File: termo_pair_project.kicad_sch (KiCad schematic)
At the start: 25 parts, among them P1 503, P2 503, U2 NE5532

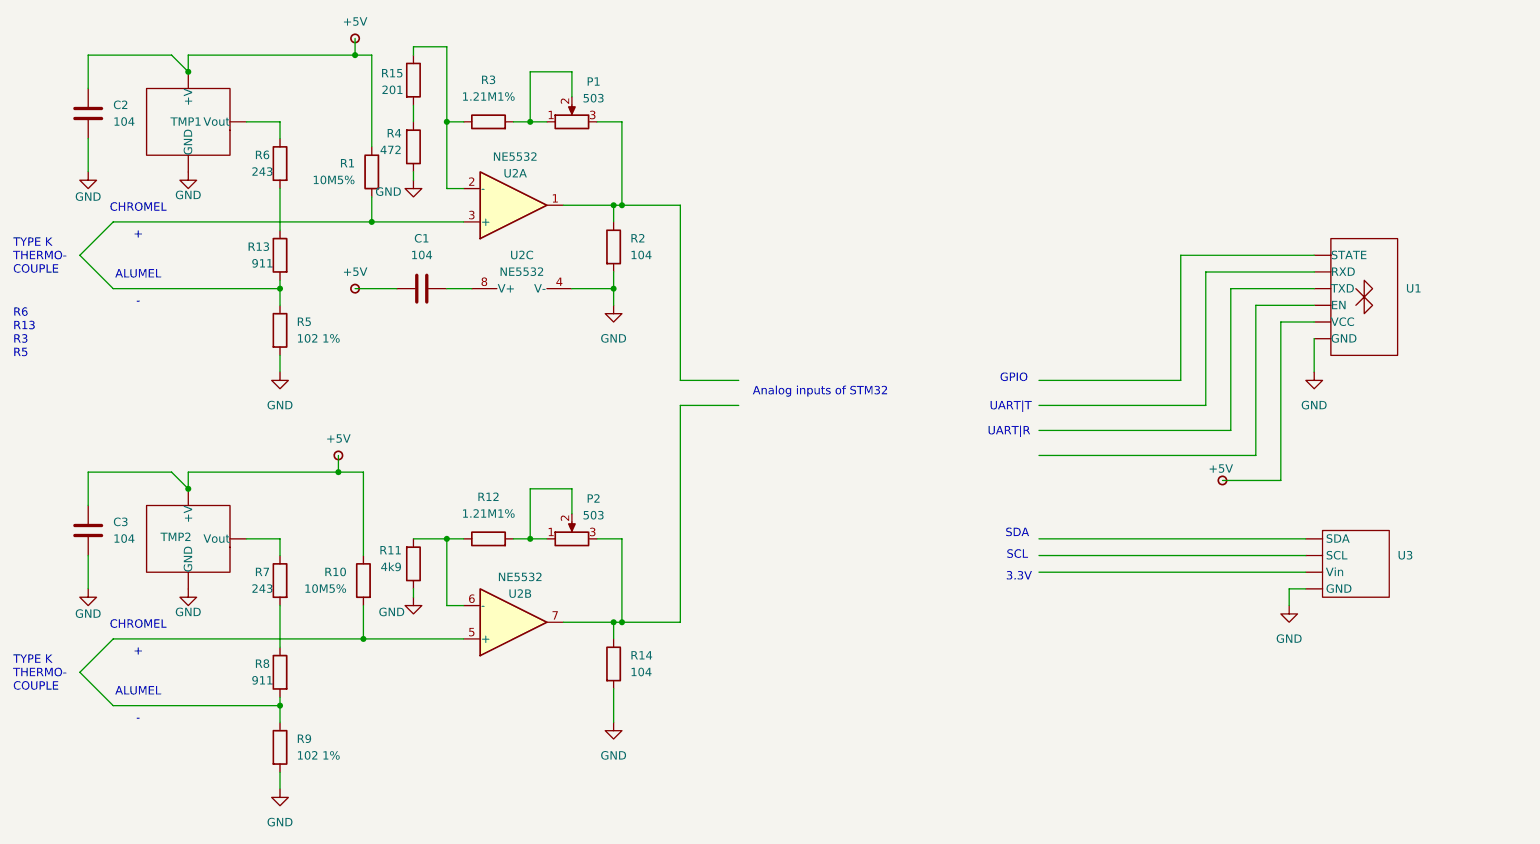
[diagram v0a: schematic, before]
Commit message: Added microcontroller to shematic
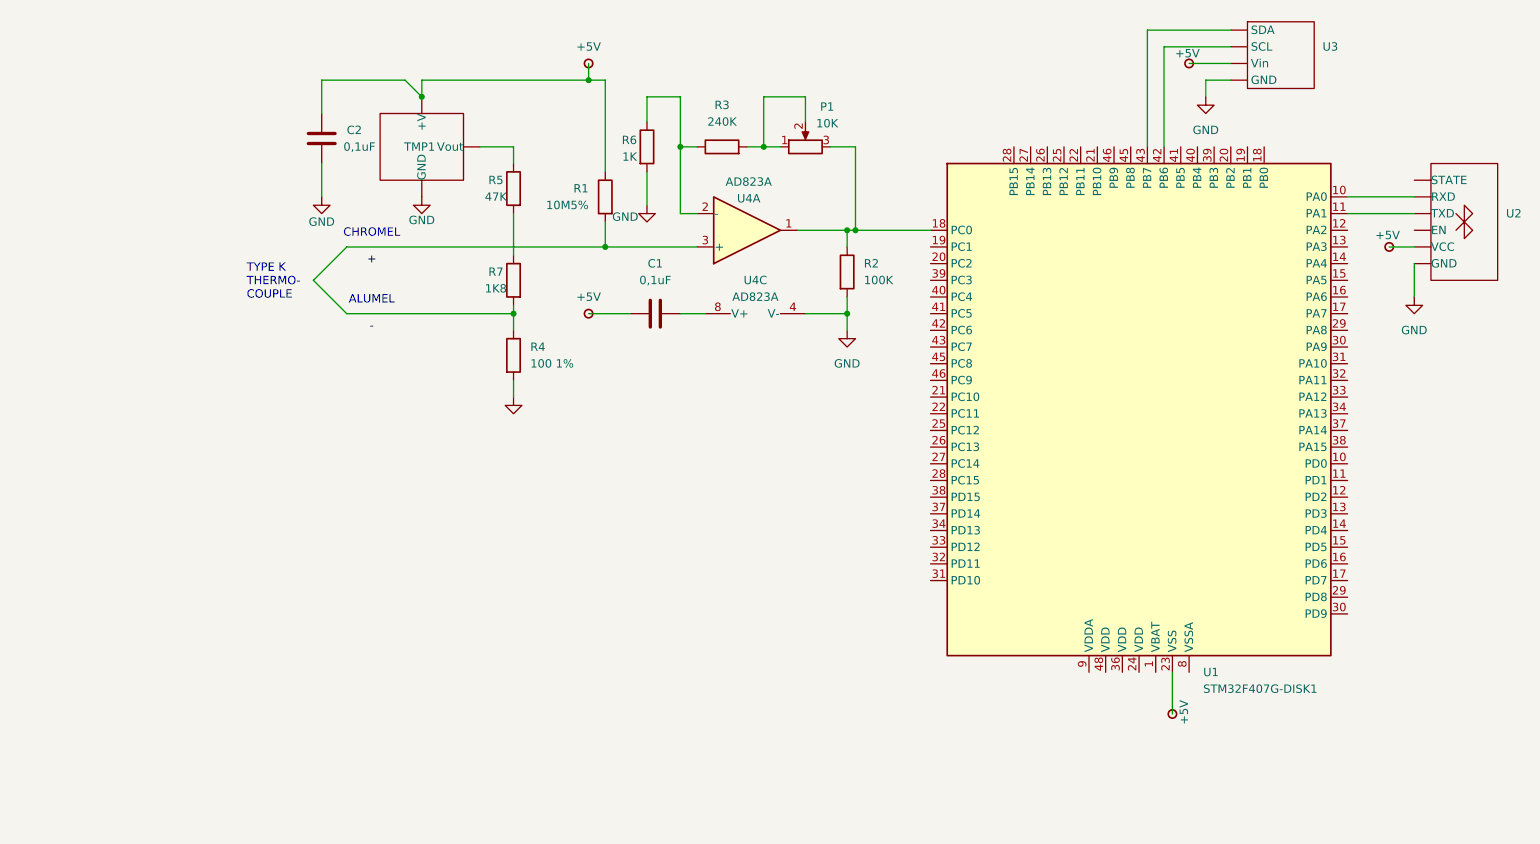
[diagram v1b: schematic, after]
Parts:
- removed C3: 104, symbol Device:C
- removed P2: 503, symbol Device:R_Potentiometer
- removed R10: 10M5%, symbol Device:R
- removed R11: 4k9, symbol Device:R
- removed R12: 1.21M1%, symbol Device:R
- removed R14: 104, symbol Device:R
- removed R4: 472, symbol Device:R
- removed R7: 243, symbol Device:R
- removed R8: 911, symbol Device:R
- removed R9: 102 1%, symbol Device:R
- removed TMP2: ~, symbol my_lib:TMP35
- removed unit 2 of U2
- added U1: STM32F407G-DISK1, Package_QFP:LQFP-48_7x7mm_P0.5mm, symbol my_lib:STM32U031C6Tx
- C1, C2: value 104 -> 0,1uF
- P1: value 503 -> 10K
- R2: value 104 -> 100K
- R3: value 1.21M1% -> 240K
- R4: renamed from R5; value 102 1% -> 100 1%
- R5: renamed from R6; value 243 -> 47K
- R6: renamed from R15; value 201 -> 1K
- R7: renamed from R13; value 911 -> 1K8
- U4: renamed from U2; value NE5532 -> AD823A
- renumbered U1 to U2
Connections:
- net +5V: now also U3. (GND), U1.23 (VSS), U1.35 (VSS), U1.47 (VSS)
- net GND: now also R6.2
- net at P1.3, R2.1, U4.1: now also U1.18 (PB0)
- new net: U1.42 (PB6), U3. (GND)
- new net: U1.43 (PB7), U3. (GND)
- new net: U1.10 (PD0), U2. (GND)
- new net: U1.11 (PD1), U2. (GND)
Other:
- note removed: "3.3V"
- note removed: "Analog inputs of STM32"
- note removed: "GPIO"
- note removed: "R6 R13 R3 R5"
- note removed: "SCL"
- note removed: "SDA"
- note removed: "UART|R"
- note removed: "UART|T"
- moved on the sheet: C1, C2, P1, R1, R2, R3, R4, R5, R6, R7, TMP1, U2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
